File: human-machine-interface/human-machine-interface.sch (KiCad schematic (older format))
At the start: 14 parts, among them J1 USB_B_Micro, J2 Conn_01x04_Male, J3 Conn_01x04_Male, SW1 SW_DPDT_x2, SW2 SW_Push, SW3 SW_Push, U1 Teensy3.2, U2 NRF24L01+ breakout

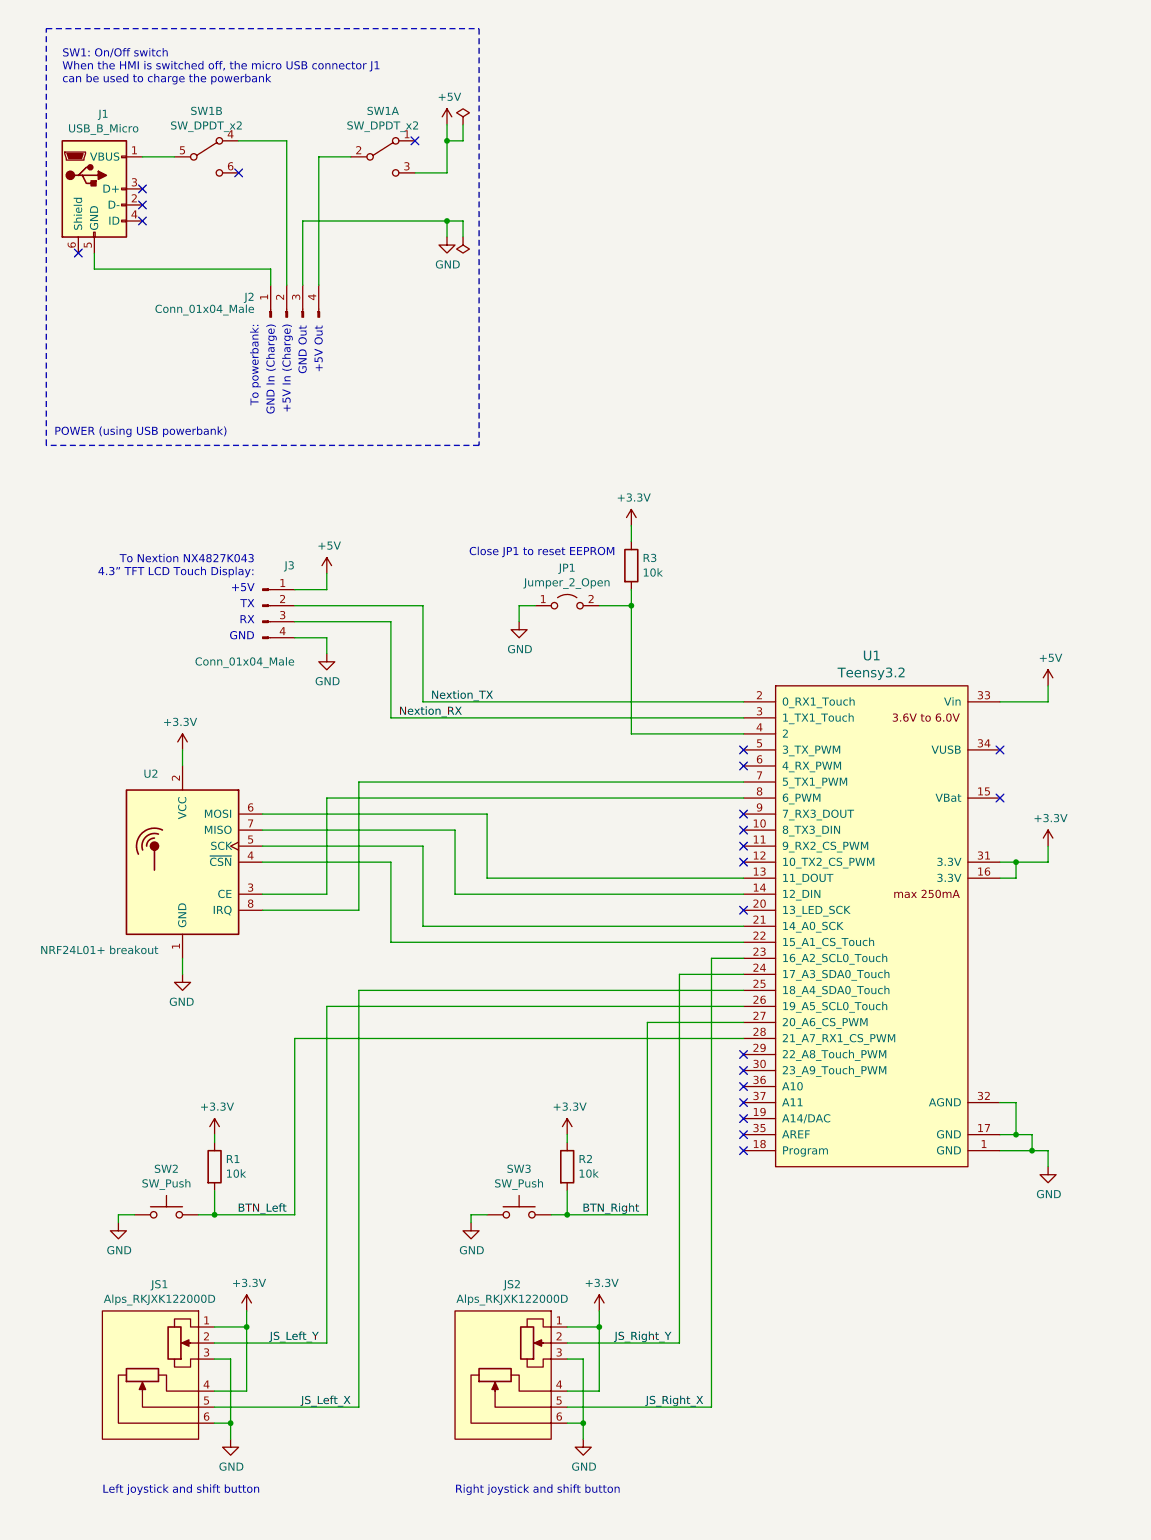
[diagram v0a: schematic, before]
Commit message: Improve layout of HMI schematic
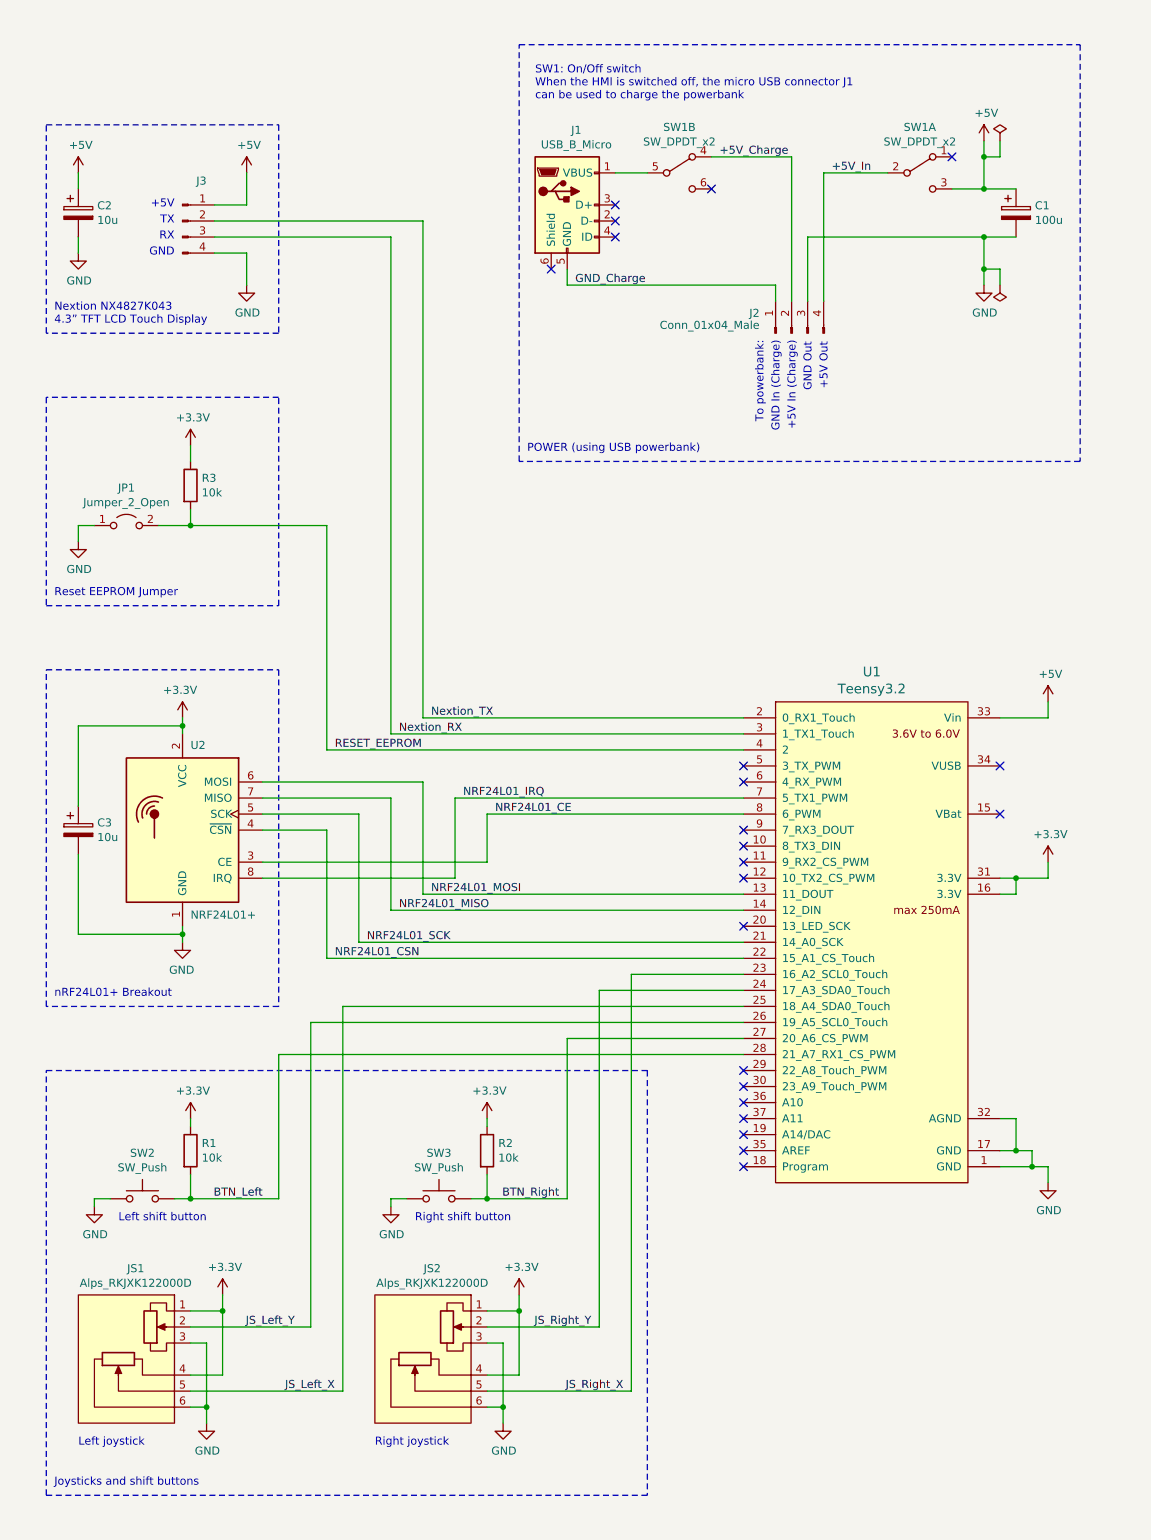
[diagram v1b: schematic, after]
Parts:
- added C1: 100u, symbol Device:CP
- added C2, C3: 10u, symbol Device:CP
- U2: value NRF24L01+ breakout -> NRF24L01+
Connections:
- net +3V3: now also C3.1
- net +5V: now also C1.1, C2.1
- net GND: now also C1.2, C2.2, C3.2
- net NRF24L01_CE: now reaches U1.8 (6_PWM), U2.3 (CE)
- net NRF24L01_CSN: now reaches U1.22 (15_A1_CS_Touch), U2.4 (~CSN)
- net NRF24L01_SCK: now reaches U1.21 (14_A0_SCK), U2.5 (SCK)
- net NRF24L01_MOSI: now reaches U1.13 (11_DOUT), U2.6 (MOSI)
- net NRF24L01_MISO: now reaches U1.14 (12_DIN), U2.7 (MISO)
- net NRF24L01_IRQ: now reaches U1.7 (5_TX1_PWM), U2.8 (IRQ)
- net GND_Charge: now reaches J1.5 (GND), J2.1 (Pin_1)
- net +5V_Charge: now reaches J2.2 (Pin_2), SW1.4 (A)
- net +5V_In: now reaches J2.4 (Pin_4), SW1.2 (B)
- net RESET_EEPROM: now reaches JP1.2 (B), R3.2, U1.4 (2)
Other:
- note added: "Joysticks and shift buttons"
- note added: "Left joystick"
- note added: "Left shift button"
- note added: "Nextion NX4827K043\n4.3” TFT LCD Touch Display"
- note added: "Reset EEPROM Jumper"
- note added: "Right joystick"
- note added: "Right shift button"
- note added: "nRF24L01+ Breakout"
- note removed: "Close JP1 to reset EEPROM"
- note removed: "Left joystick and shift button"
- note removed: "Right joystick and shift button"
- note removed: "To Nextion NX4827K043\n4.3” TFT LCD Touch Display:"
- moved on the sheet: J1, J2, J3, JP1, JS1, JS2, R1, R2, R3, SW1A, SW1B, SW2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

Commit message: Add (optional) GPS receiver to HMI schematic
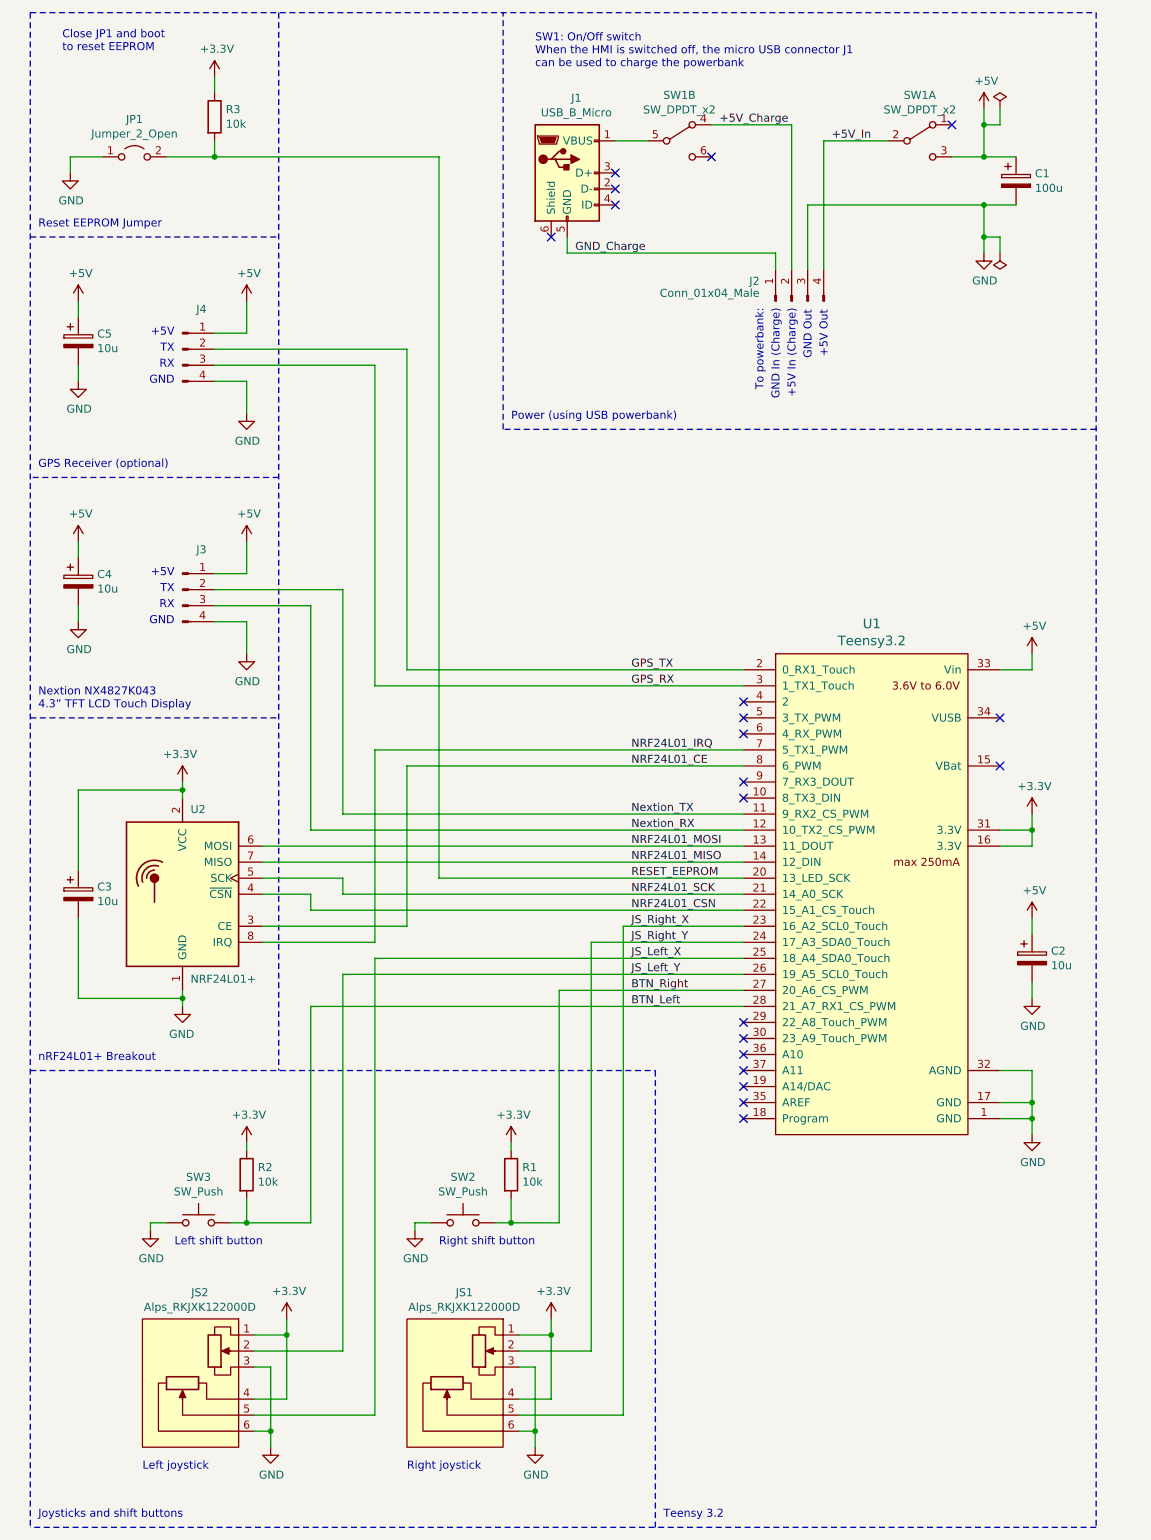
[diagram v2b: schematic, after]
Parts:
- added C2, C4: 10u, symbol Device:CP
- added J3: Conn_01x04_Male, symbol Connector:Conn_01x04_Male
- renumbered C2 to C5, J3 to J4, JS2 to JS1, JS1 to JS2, R2 to R1, R1 to R2, SW3 to SW2, SW2 to SW3
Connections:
- net +5V: now also C2.1, C4.1, J3.1 (Pin_1)
- net GND: now also C2.2, C4.2, J3.4 (Pin_4)
- net Nextion_RX: now also U1.12 (10_TX2_CS_PWM), J3.3 (Pin_3); no longer J4.3 (Pin_3), U1.3 (1_TX1_Touch)
- net Nextion_TX: now also U1.11 (9_RX2_CS_PWM), J3.2 (Pin_2); no longer J4.2 (Pin_2), U1.2 (0_RX1_Touch)
- net RESET_EEPROM: now also U1.20 (13_LED_SCK); no longer U1.4 (2)
- new net GPS_RX: J4.3 (Pin_3), U1.3 (1_TX1_Touch)
- new net GPS_TX: J4.2 (Pin_2), U1.2 (0_RX1_Touch)
- no-connect marks 22 -> 20
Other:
- note added: "Close JP1 and boot\nto reset EEPROM"
- note added: "GPS Receiver (optional)"
- note added: "Power (using USB powerbank)"
- note added: "Teensy 3.2"
- note removed: "POWER (using USB powerbank)"
- moved on the sheet: C1, C3, C5, J1, J2, J4, JP1, JS1, JS2, R1, R2, R3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

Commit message: Improve layouts and add capacitors
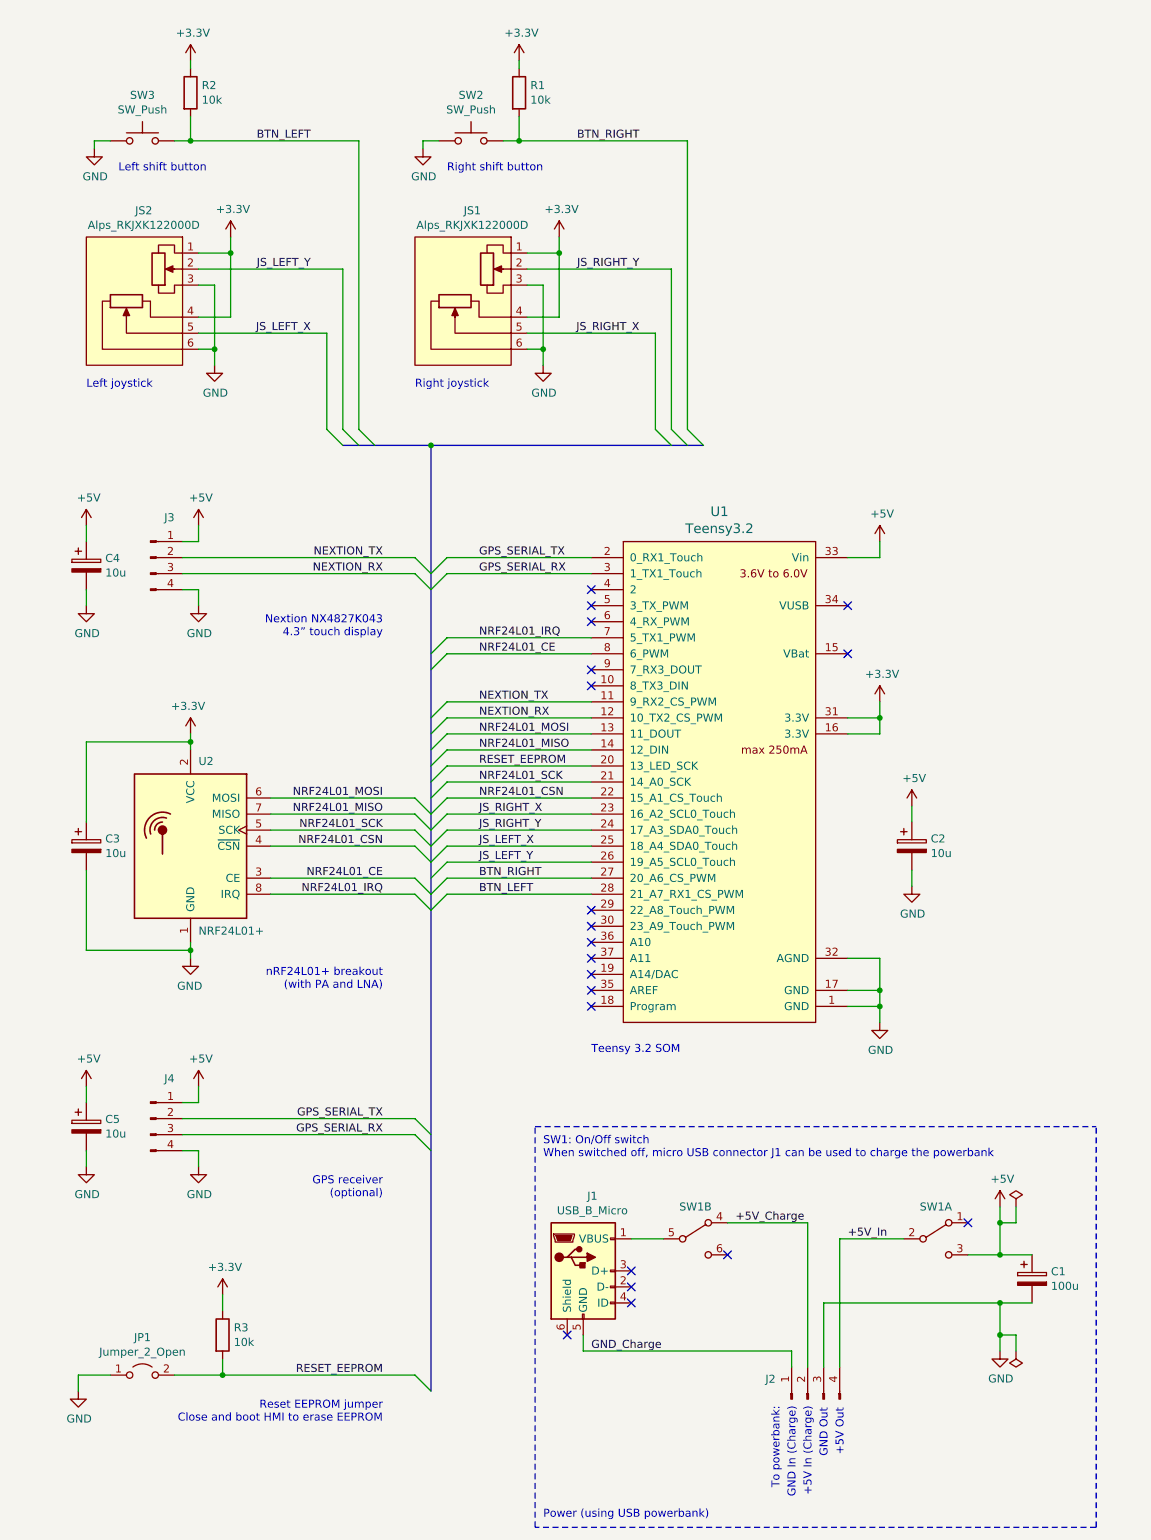
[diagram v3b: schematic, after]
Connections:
- net BTN_Left renamed BTN_LEFT
- net BTN_Right renamed BTN_RIGHT
- net GPS_RX renamed GPS_SERIAL_RX
- net GPS_TX renamed GPS_SERIAL_TX
- net JS_Left_X renamed JS_LEFT_X
- net JS_Left_Y renamed JS_LEFT_Y
- net JS_Right_X renamed JS_RIGHT_X
- net JS_Right_Y renamed JS_RIGHT_Y
- net Nextion_RX renamed NEXTION_RX
- net Nextion_TX renamed NEXTION_TX
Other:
- note added: "GPS receiver\n(optional)"
- note added: "Nextion NX4827K043\n4.3” touch display"
- note added: "Reset EEPROM jumper\nClose and boot HMI to erase EEPROM"
- note added: "SW1: On/Off switch\nWhen switched off, micro USB connector J1 can be used to charge the powerbank"
- note added: "Teensy 3.2 SOM"
- note added: "nRF24L01+ breakout\n(with PA and LNA)"
- note removed: "+5V"
- note removed: "Close JP1 and boot\nto reset EEPROM"
- note removed: "GND"
- note removed: "GPS Receiver (optional)"
- note removed: "Joysticks and shift buttons"
- note removed: "Nextion NX4827K043\n4.3” TFT LCD Touch Display"
- note removed: "RX"
- note removed: "Reset EEPROM Jumper"
- note removed: "SW1: On/Off switch\nWhen the HMI is switched off, the micro USB connector J1\ncan be used to charge the powerbank"
- note removed: "TX"
- note removed: "Teensy 3.2"
- note removed: "nRF24L01+ Breakout"
- moved on the sheet: C1, C2, C3, C4, C5, J1, J2, J3, J4, JP1, JS1, JS2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

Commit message: Add Alps Alpine ThumbPointer RKJXK122000D footprint
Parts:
- JS1, JS2: footprint (none) -> earth-rover-custom-footprints:Alps_RKJXK122000D
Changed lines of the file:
@@
 EESchema Schematic File Version 4
-LIBS:human-machine-interface-cache
 EELAYER 30 0
 EELAYER END
@@
 F 0 "JS1" H 3642 2365 50  0000 C CNN
 F 1 "Alps_RKJXK122000D" H 3642 2274 50  0000 C CNN
-F 2 "" H 3750 1775 50  0001 C CNN
+F 2 "earth-rover-custom-footprints:Alps_RKJXK122000D" H 3750 1775 50  0001 C CNN
 F 3 "https://www.alps.com/prod/info/E/HTML/MultiControl/Potentiometer/RKJXK/RKJXK122000D.html" H 3750 1775 50  0001 C CNN
 	1    3700 2100
@@
 F 0 "JS2" H 1592 2365 50  0000 C CNN
 F 1 "Alps_RKJXK122000D" H 1592 2274 50  0000 C CNN
-F 2 "" H 1700 1775 50  0001 C CNN
+F 2 "earth-rover-custom-footprints:Alps_RKJXK122000D" H 1700 1775 50  0001 C CNN
 F 3 "https://www.alps.com/prod/info/E/HTML/MultiControl/Potentiometer/RKJXK/RKJXK122000D.html" H 1700 1775 50  0001 C CNN
 	1    1650 2100
@@
 F 0 "U1" H 5300 4287 60  0000 C CNN
 F 1 "Teensy3.2" H 5300 4181 60  0000 C CNN
-F 2 "" H 8100 2850 60  0000 C CNN
+F 2 "" H 8100 2850 60  0001 C CNN
 F 3 "" H 8100 2850 60  0000 C CNN
 	1    4700 4000
@@
 Wire Wire Line
 	4100 2600 4900 2600
+Text Notes 4500 7100 0    50   ~ 0
+Teensy 3.2 SOM
 Wire Bus Line
 	2950 3300 3500 3300
@@
 Wire Bus Line
 	3500 3300 3500 9200
-Text Notes 4500 7100 0    50   ~ 0
-Teensy 3.2 SOM
 $EndSCHEMATC
